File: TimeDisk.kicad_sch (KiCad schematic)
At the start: 72 parts, among them J1 AppleIIBus, J2 microUSB, J3 JTAG, SW1 Mode, U1 EPM7128SL84, U2 DS1315S-5, U3 74LVC04AD, U4 AS6C8008, U5 39F040, U6 XC6206P332MR, U7 CH340G, U8 74LVC1G74DC, U9 74AHCT1G125GW, Y1 32k768, Y2 12M

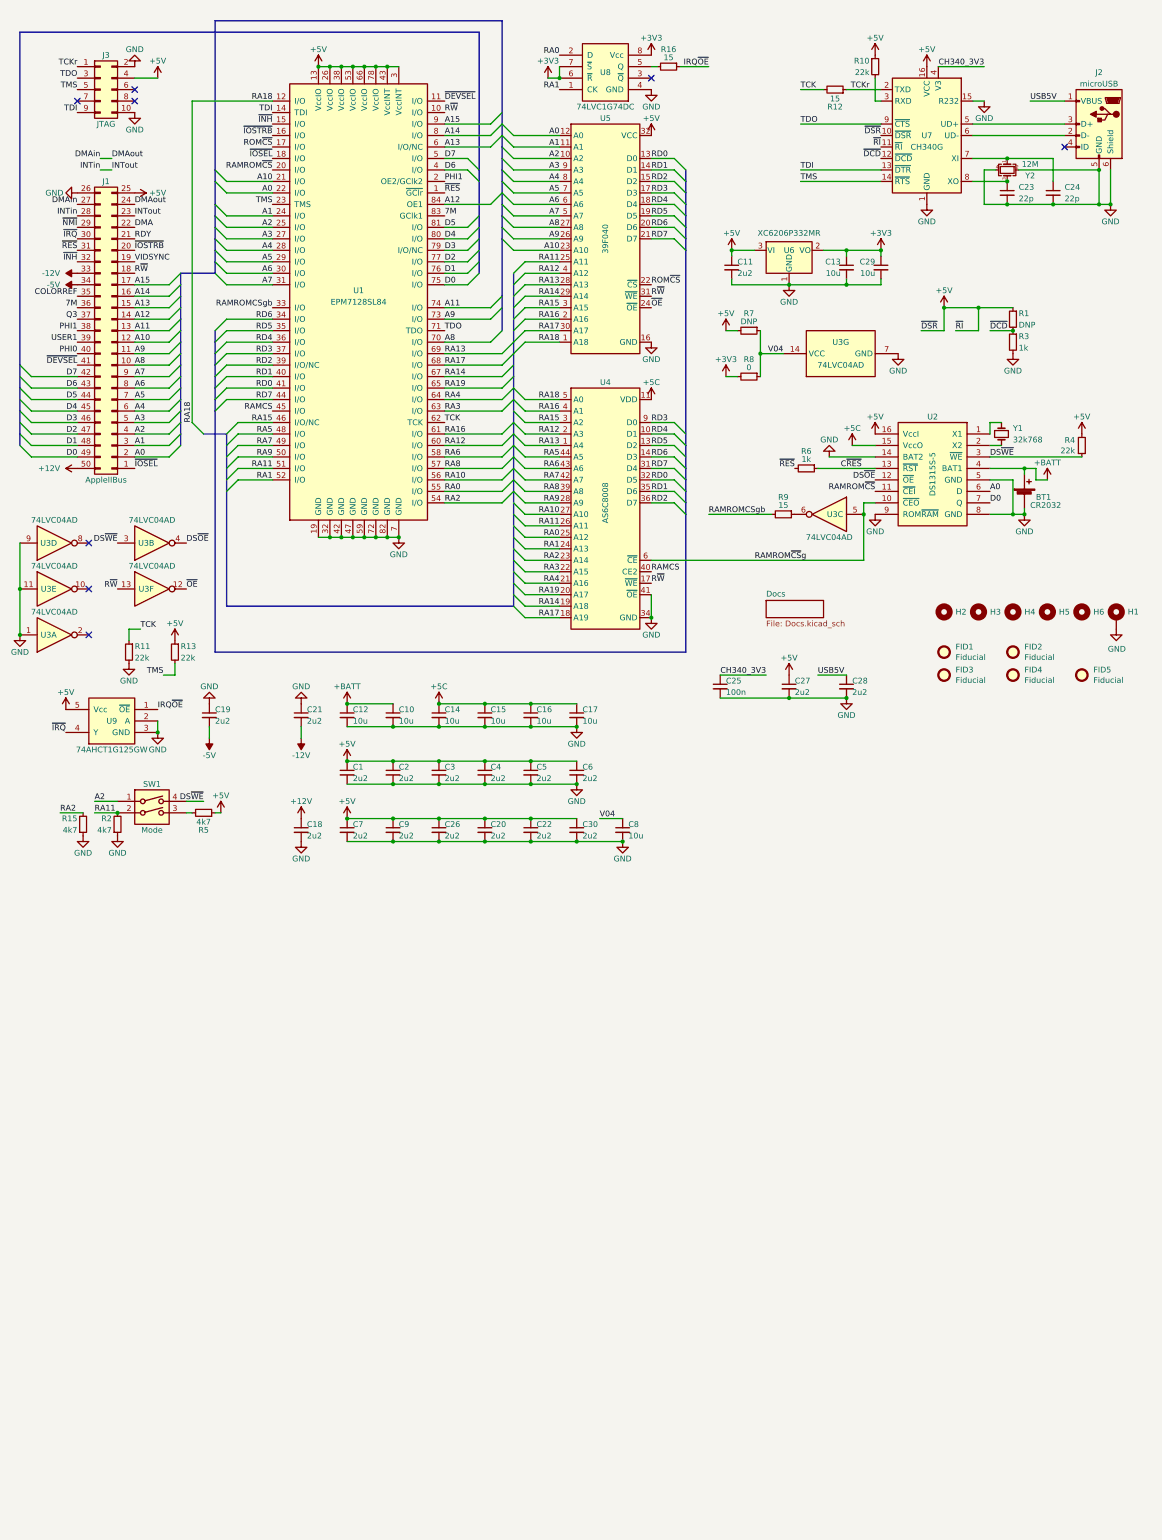
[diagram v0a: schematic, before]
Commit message: Start C revision
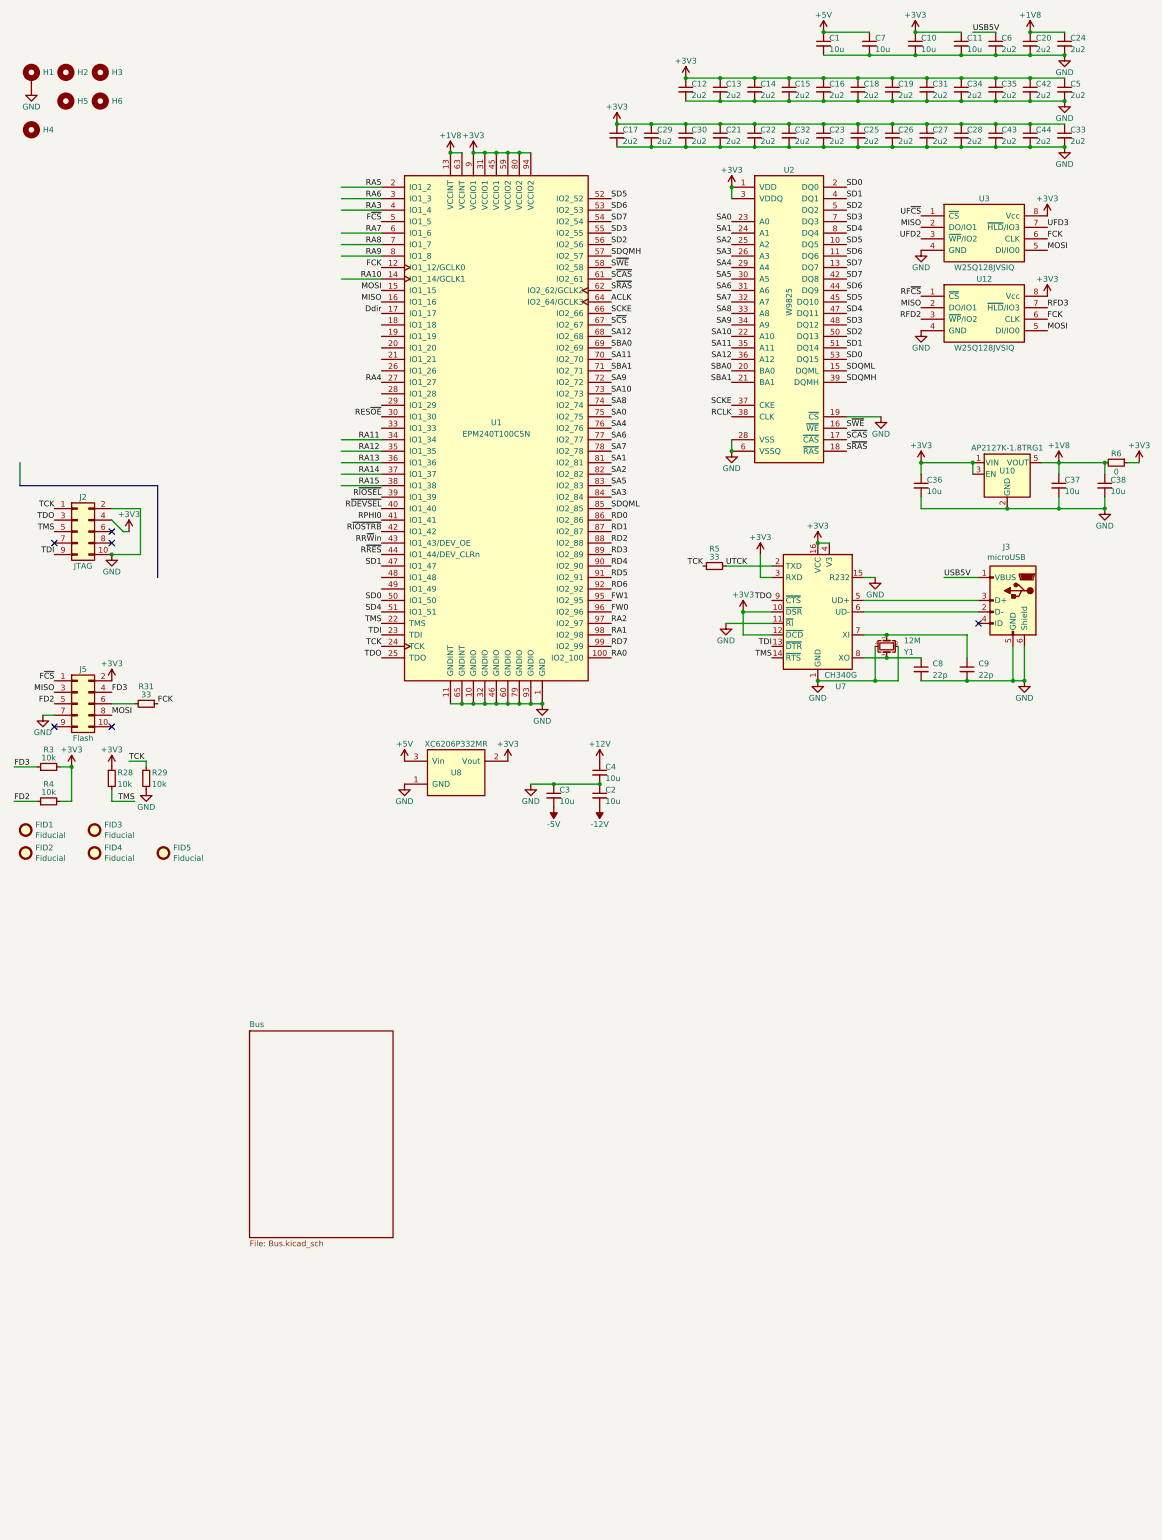
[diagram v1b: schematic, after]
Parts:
- removed BT1: CR2032, stdpads:Keystone_3034_2032, symbol Device:Battery_Cell
- removed C2, C3, C4: 2u2, stdpads:C_0805, symbol Device:C_Small
- removed J1: AppleIIBus, stdpads:AppleIIBus_Edge, symbol Connector_Generic:Conn_02x25_Counter_Clockwise
- removed J2: microUSB, stdpads:USB_Micro-B_Amphenol_10118192-0001, symbol Connector:USB_B_Micro
- removed J3: JTAG, stdpads:Header_2x5_Unshrouded_P1.27mm, symbol Connector_Generic:Conn_02x05_Odd_Even
- removed R1, R7: DNP, stdpads:R_0805, symbol Device:R_Small
- removed R10, R11, R13: 22k, stdpads:R_0805, symbol Device:R_Small
- removed R12, R16, R9: 15, stdpads:R_0805, symbol Device:R_Small
- removed R15, R2: 4k7, stdpads:R_0805, symbol Device:R_Small
- removed R8: 0, stdpads:R_0805, symbol Device:R_Small
- removed SW1: Mode, stdpads:SW_DIP_SPSTx02_Slide_DSHP02TS_P1.27mm, symbol Switch:SW_DIP_x02
- removed U1: EPM7128SL84, stdpads:PLCC-84, symbol GW_PLD:EPM7128SL84
- removed U2: DS1315S-5, stdpads:SOIC-16_7.5mm, symbol GW_Digital:DS1315
- removed U3: 74LVC04AD, stdpads:SOIC-14_3.9mm, symbol 74xx:74HC04
- removed U4: AS6C8008, stdpads:TSOP-II-44_400mil_P0.8mm, symbol GW_RAM:SRAM-1Mx8-TSOP2-44
- removed U5: 39F040, stdpads:PLCC-32_SMDSocket, symbol GW_RAM:Flash-512Kx8-PLCC-32
- removed U6: XC6206P332MR, stdpads:SOT-23, symbol Regulator_Linear:XC6206PxxxMR
- removed U8: 74LVC1G74DC, stdpads:NXP_VSSOP-8_2.3x2mm, symbol GW_Logic:741G74DC
- removed U9: 74AHCT1G125GW, stdpads:SOT-353, symbol GW_Logic:741G125GW
- removed Y1: 32k768, Crystal:Crystal_C26-LF_D2.1mm_L6.5mm_Horizontal, symbol Device:Crystal_Small
- removed Y2: 12M, stdpads:Crystal_SMD_3225-4Pin_3.2x2.5mm, symbol Device:Crystal_GND24_Small
- added C18, C19, C21, C31, C32, C33, C34, C35, C42, C43, C44: 2u2, stdpads:C_0603, symbol Device:C_Small
- added C36, C37, C38: 10u, stdpads:C_0805, symbol Device:C_Small
- added J2: JTAG, Connector:Tag-Connect_TC2050-IDC-FP_2x05_P1.27mm_Vertical, symbol Connector_Generic:Conn_02x05_Odd_Even
- added J3: microUSB, stdpads:USB_Micro-B_Amphenol_10118192-0001, symbol Connector:USB_B_Micro
- added J5: Flash, Connector:Tag-Connect_TC2050-IDC-FP_2x05_P1.27mm_Vertical, symbol Connector_Generic:Conn_02x05_Odd_Even
- added R28, R29: 10k, stdpads:R_0603, symbol Device:R_Small
- added R31: 33, stdpads:R_0603, symbol Device:R_Small
- added U1: EPM240T100C5N, stdpads:TQFP-100_14x14mm_P0.5mm, symbol GW_PLD:5M240ZT100
- added U10: AP2127K-1.8TRG1, stdpads:SOT-23-5, symbol Regulator_Linear:AP2127K-1.8
- added U12, U3: W25Q128JVSIQ, stdpads:SOIC-8_5.3mm, symbol GW_RAM:SPIFlash-SO-8
- added U2: W9825, stdpads:TSOP-II-54_22.2x10.16mm_P0.8mm, symbol GW_RAM:SDRAM-16Mx16-TSOP2-54
- added U8: XC6206P332MR, stdpads:SOT-23, symbol GW_Power:AP2125
- added Y1: 12M, stdpads:Crystal_SMD_3225-4Pin_3.2x2.5mm, symbol Device:Crystal_GND24_Small
- C1, C11, C7: value 2u2 -> 10u; LCSC Part (none) -> C15850
- C10: LCSC Part (none) -> C15850
- C12, C13, C14, C15, C16, C17, C29: value 10u -> 2u2; footprint stdpads:C_0805 -> stdpads:C_0603; LCSC Part (none) -> C23630
- C2: renamed from C21; value 2u2 -> 10u; LCSC Part (none) -> C15850
- C20, C22, C26, C30, C5, C6: footprint stdpads:C_0805 -> stdpads:C_0603; LCSC Part (none) -> C23630
- C23, C24: value 22p -> 2u2; LCSC Part C1653 -> C23630
- C25: value 100n -> 2u2; LCSC Part C28233 -> C23630
- C27, C28: footprint stdpads:C_0805 -> stdpads:C_0603
- C3: renamed from C19; value 2u2 -> 10u; LCSC Part (none) -> C15850
- C4: renamed from C18; value 2u2 -> 10u; LCSC Part (none) -> C15850
- C8: value 10u -> 22p; footprint stdpads:C_0805 -> stdpads:C_0603; LCSC Part (none) -> C1653
- C9: value 2u2 -> 22p; footprint stdpads:C_0805 -> stdpads:C_0603; LCSC Part (none) -> C1653
- R3: value 1k -> 10k; footprint stdpads:R_0805 -> stdpads:R_0603; LCSC Part (none) -> 10k
- R4: value 22k -> 10k; footprint stdpads:R_0805 -> stdpads:R_0603; LCSC Part (none) -> 10k
- R5: value 4k7 -> 33; footprint stdpads:R_0805 -> stdpads:R_0603; LCSC Part (none) -> C23140
- R6: value 1k -> 0; LCSC Part (none) -> C17477; Mfg. Part Numbers (none) -> Uniroyal 0805W8F0000T5E; Notes (none) -> Any manufacturer's part is acceptable.
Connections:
- net +5C is gone; now on net +3V3: C14.1, C15.1, C16.1, C17.1
- net +BATT is gone; now on net +3V3: C10.1, C12.1
- net CH340_3V3 is gone; now on net +3V3: C25.1, U7.4 (V3)
- net C~{RES} is gone; now on net +3V3: R6.1
- net V04 is gone; now on an unnamed net: C8.1
- net +3V3: now also C11.1, C22.1, C23.1, C26.1, C27.1, C28.1, C30.1, C5.1, R3.2, R4.2, U7.10 (~{DSR}), U7.12 (~{DCD}), U7.16 (VCC), U7.3 (RXD), C18.1, C19.1, C21.1, C31.1, C32.1, C33.1, C34.1, C35.1, C36.1, C42.1, C43.1, C44.1, J2.4 (Pin_4), J5.2 (Pin_2), R28.1, U1.31 (VCCIO1), U1.45 (VCCIO1), U1.59 (VCCIO2), U1.80 (VCCIO2), U1.9 (VCCIO1), U1.94 (VCCIO2), U10.1 (VIN), U10.3 (EN), U12.8 (Vcc), U2.1 (VDD), U2.14 (VDD), U2.27 (VDD), U2.3 (VDDQ), U2.43 (VDDQ), U2.49 (VDDQ), U2.9 (VDDQ), U3.8 (Vcc), U8.2 (Vout)
- net +5V: now also U8.3 (Vin); no longer C11.1, C20.1, C22.1, C26.1, C27.1, C30.1, C5.1, C6.1, C9.1, R4.2, R5.1, U7.10 (~{DSR}), U7.11 (~{RI}), U7.16 (VCC)
- net GND: now also U7.11 (~{RI}), C18.2, C19.2, C21.2, C31.2, C32.2, C33.2, C34.2, C35.2, C36.2, C37.2, C38.2, C42.2, C43.2, C44.2, J2.10 (Pin_10), J2.2 (Pin_2), J3.5 (GND), J3.6 (Shield), J5.7 (Pin_7), R29.2, U1.1 (GND), U1.10 (GNDIO), U1.11 (GNDINT), U1.32 (GNDIO), U1.46 (GNDIO), U1.60 (GNDIO), U1.65 (GNDINT), U1.79 (GNDIO), U1.93 (GNDIO), U10.2 (GND), U12.4 (GND), U2.12 (VSSQ), U2.19 (~{CS}), U2.28 (VSS), U2.41 (VSS), U2.46 (VSSQ), U2.52 (VSSQ), U2.54 (VSS), U2.6 (VSSQ), U3.4 (GND), U8.1 (GND), Y1.2, Y1.4; no longer R3.2
- net RA0: now also U1.100 (IO2_100)
- net RA1: now also U1.98 (IO2_98)
- net RA10: now also U1.14 (IO1_14/GCLK1)
- net RA11: now also U1.34 (IO1_34)
- net RA12: now also U1.35 (IO1_35)
- net RA13: now also U1.36 (IO1_36)
- net RA14: now also U1.37 (IO1_37)
- net RA15: now also U1.38 (IO1_38)
- net RA2: now also U1.97 (IO2_97)
- net RA3: now also U1.4 (IO1_4)
- net RA4: now also U1.27 (IO1_27)
- net RA5: now also U1.2 (IO1_2)
- net RA6: now also U1.3 (IO1_3)
- net RA7: now also U1.6 (IO1_6)
- net RA8: now also U1.7 (IO1_7)
- net RA9: now also U1.8 (IO1_8)
- net RD0: now also U1.86 (IO2_86)
- net RD1: now also U1.87 (IO2_87)
- net RD2: now also U1.88 (IO2_88)
- net RD3: now also U1.89 (IO2_89)
- net RD4: now also U1.90 (IO2_90)
- net RD5: now also U1.91 (IO2_91)
- net RD6: now also U1.92 (IO2_92)
- net RD7: now also U1.99 (IO2_99)
- net TCK: now also R5.2, J2.1 (Pin_1), R29.1, U1.24 (TCK)
- net TDI: now also J2.9 (Pin_9), U1.23 (TDI)
- net TDO: now also J2.3 (Pin_3), U1.25 (TDO)
- net TMS: now also J2.5 (Pin_5), R28.2, U1.22 (TMS)
- net USB5V: now also C6.1, J3.1 (VBUS); no longer C28.1
- net at U7.6 (UD-): now also J3.2 (D-)
- net at U7.5 (UD+): now also J3.3 (D+)
- net at U7.7 (XI): now also C9.1, Y1.1; no longer C24.1
- net at U7.8 (XO): now also Y1.3; no longer C23.1
- net DS~{WE} renamed FD2
- net FD2: now also J5.5 (Pin_5)
- net TCKr renamed UTCK
- net UTCK: now also R5.1
- net ~{DCD} renamed FD3
- net FD3: now also J5.4 (Pin_4); no longer U7.12 (~{DCD})
- net ~{RES} renamed +1V8
- net +1V8: now also C20.1, C24.1, C37.1, C38.1, U1.13 (VCCINT), U1.63 (VCCINT), U10.5 (VOUT)
- new net: J5.6 (Pin_6), R31.2
- new net ACLK: U1.64 (IO2_64/GCLK3)
- new net Ddir: U1.17 (IO1_17)
- new net FCK: R31.1, U1.12 (IO1_12/GCLK0), U12.6 (CLK), U3.6 (CLK)
- new net FW0: U1.96 (IO2_96)
- new net FW1: U1.95 (IO2_95)
- new net F~{CS}: J5.1 (Pin_1), U1.5 (IO1_5)
- new net MISO: J5.3 (Pin_3), U1.16 (IO1_16), U12.2 (DO/IO1), U3.2 (DO/IO1)
- new net MOSI: J5.8 (Pin_8), U1.15 (IO1_15), U12.5 (DI/IO0), U3.5 (DI/IO0)
- new net RCLK: U2.38 (CLK)
- new net RES~{OE}: U1.30 (IO1_30)
- new net RFD2: U12.3 (~{WP}/IO2)
- new net RFD3: U12.7 (~{HLD}/IO3)
- new net RF~{CS}: U12.1 (~{CS})
- new net RPHI0: U1.41 (IO1_41)
- new net RR~{W}in: U1.43 (IO1_43/DEV_OE)
- new net R~{DEVSEL}: U1.40 (IO1_40)
- new net R~{IOSEL}: U1.39 (IO1_39)
- new net R~{IOSTRB}: U1.42 (IO1_42)
- new net R~{RES}: U1.44 (IO1_44/DEV_CLRn)
- new net SA0: U1.75 (IO2_75), U2.23 (A0)
- new net SA1: U1.81 (IO2_81), U2.24 (A1)
- new net SA10: U1.73 (IO2_73), U2.22 (A10)
- new net SA11: U1.70 (IO2_70), U2.35 (A11)
- new net SA12: U1.68 (IO2_68), U2.36 (A12)
- new net SA2: U1.82 (IO2_82), U2.25 (A2)
- new net SA3: U1.84 (IO2_84), U2.26 (A3)
- new net SA4: U1.76 (IO2_76), U2.29 (A4)
- new net SA5: U1.83 (IO2_83), U2.30 (A5)
- new net SA6: U1.77 (IO2_77), U2.31 (A6)
- new net SA7: U1.78 (IO2_78), U2.32 (A7)
- new net SA8: U1.74 (IO2_74), U2.33 (A8)
- new net SA9: U1.72 (IO2_72), U2.34 (A9)
- new net SBA0: U1.69 (IO2_69), U2.20 (BA0)
- new net SBA1: U1.71 (IO2_71), U2.21 (BA1)
- new net SCKE: U1.66 (IO2_66), U2.37 (CKE)
- new net SD0: U1.50 (IO1_50), U2.2 (DQ0), U2.53 (DQ15)
- new net SD1: U1.47 (IO1_47), U2.4 (DQ1), U2.51 (DQ14)
- new net SD2: U1.56 (IO2_56), U2.5 (DQ2), U2.50 (DQ13)
- new net SD3: U1.55 (IO2_55), U2.48 (DQ12), U2.7 (DQ3)
- new net SD4: U1.51 (IO1_51), U2.47 (DQ11), U2.8 (DQ4)
- new net SD5: U1.52 (IO2_52), U2.10 (DQ5), U2.45 (DQ10)
- new net SD6: U1.53 (IO2_53), U2.11 (DQ6), U2.44 (DQ9)
- new net SD7: U1.54 (IO2_54), U2.13 (DQ7), U2.42 (DQ8)
- new net SDQMH: U1.57 (IO2_57), U2.39 (DQMH)
- new net SDQML: U1.85 (IO2_85), U2.15 (DQML)
- new net S~{CAS}: U1.61 (IO2_61), U2.17 (~{CAS})
- new net S~{CS}: U1.67 (IO2_67)
- new net S~{RAS}: U1.62 (IO2_62/GCLK2), U2.18 (~{RAS})
- new net S~{WE}: U1.58 (IO2_58), U2.16 (~{WE})
- new net UFD2: U3.3 (~{WP}/IO2)
- new net UFD3: U3.7 (~{HLD}/IO3)
- new net UF~{CS}: U3.1 (~{CS})
- no-connect marks 8 -> 6
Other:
- removed sheet Docs
- added sheet Bus (Bus.kicad_sch)
- title: Time Machine -> GR8RAM
- moved on the sheet: C2, C3, C4

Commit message: Start on hibernate
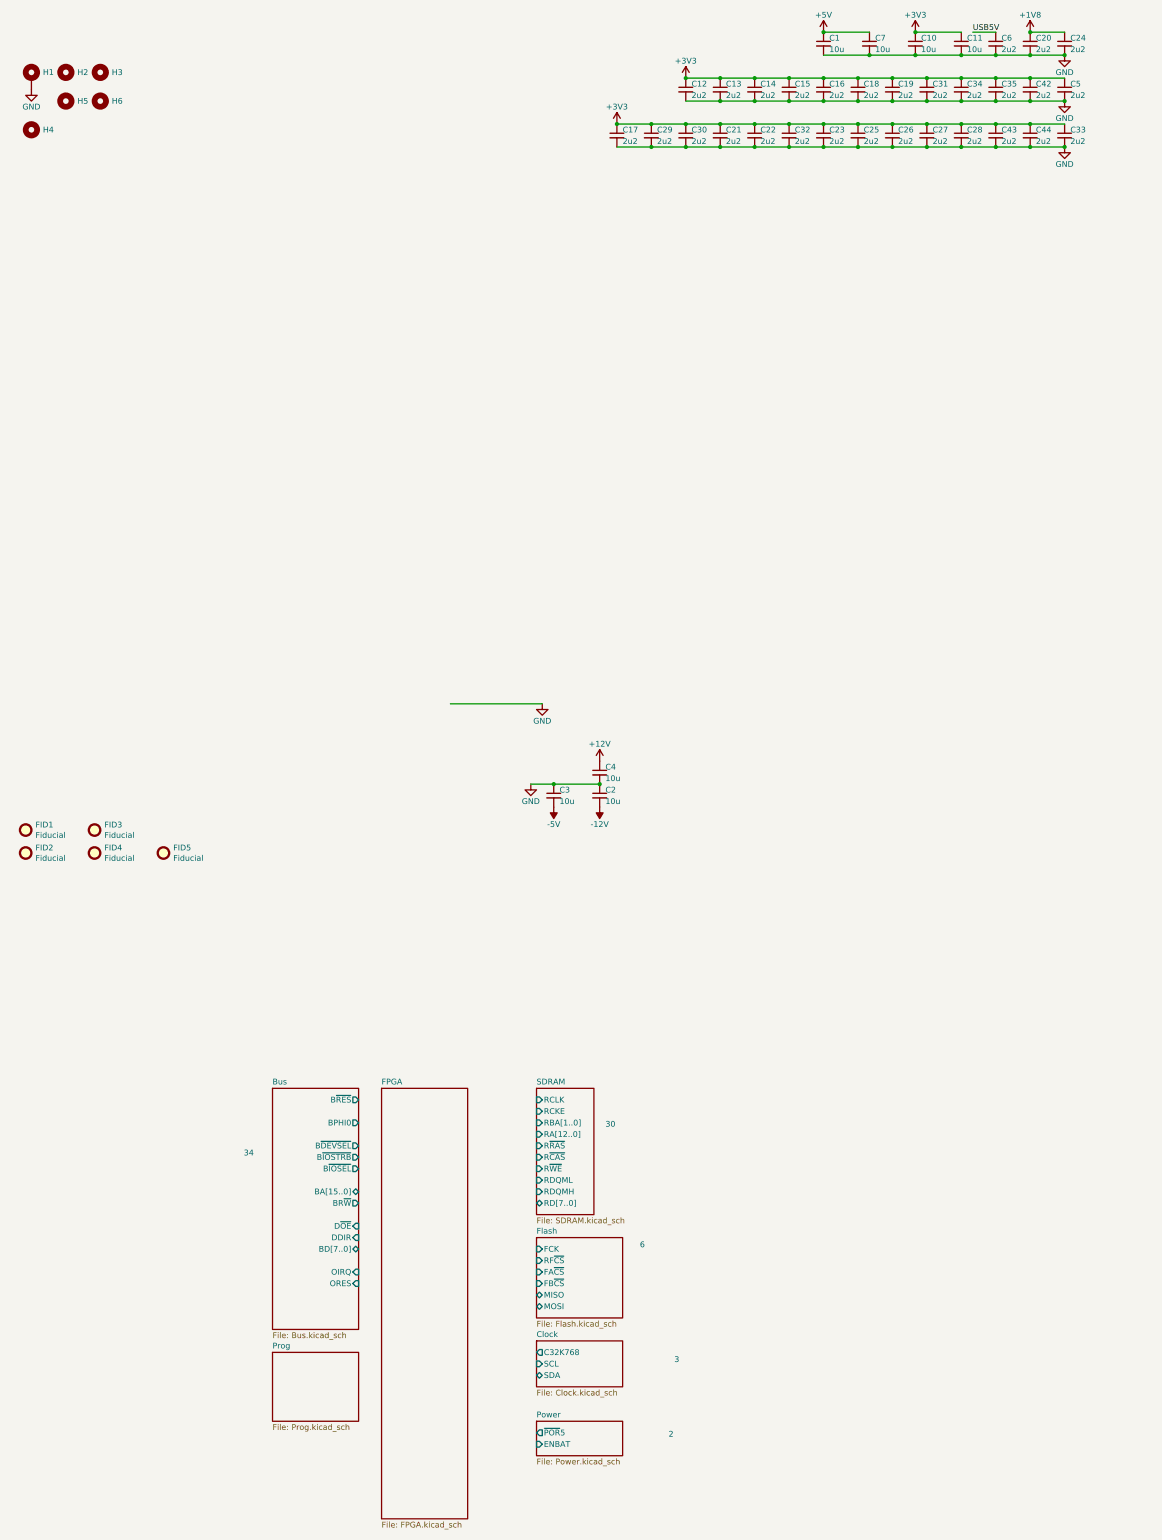
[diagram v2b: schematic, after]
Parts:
- removed C36, C37, C38: 10u, stdpads:C_0805, symbol Device:C_Small
- removed C8, C9: 22p, stdpads:C_0603, symbol Device:C_Small
- removed J2: JTAG, Connector:Tag-Connect_TC2050-IDC-FP_2x05_P1.27mm_Vertical, symbol Connector_Generic:Conn_02x05_Odd_Even
- removed J3: microUSB, stdpads:USB_Micro-B_Amphenol_10118192-0001, symbol Connector:USB_B_Micro
- removed J5: Flash, Connector:Tag-Connect_TC2050-IDC-FP_2x05_P1.27mm_Vertical, symbol Connector_Generic:Conn_02x05_Odd_Even
- removed R28, R29, R3, R4: 10k, stdpads:R_0603, symbol Device:R_Small
- removed R31, R5: 33, stdpads:R_0603, symbol Device:R_Small
- removed R6: 0, stdpads:R_0805, symbol Device:R_Small
- removed U1: EPM240T100C5N, stdpads:TQFP-100_14x14mm_P0.5mm, symbol GW_PLD:5M240ZT100
- removed U10: AP2127K-1.8TRG1, stdpads:SOT-23-5, symbol Regulator_Linear:AP2127K-1.8
- removed U12, U3: W25Q128JVSIQ, stdpads:SOIC-8_5.3mm, symbol GW_RAM:SPIFlash-SO-8
- removed U2: W9825, stdpads:TSOP-II-54_22.2x10.16mm_P0.8mm, symbol GW_RAM:SDRAM-16Mx16-TSOP2-54
- removed U7: CH340G, stdpads:SOIC-16_3.9mm, symbol Interface_USB:CH340G
- removed U8: XC6206P332MR, stdpads:SOT-23, symbol GW_Power:AP2125
- removed Y1: 12M, stdpads:Crystal_SMD_3225-4Pin_3.2x2.5mm, symbol Device:Crystal_GND24_Small
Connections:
- no-connect marks 6 -> 0
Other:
- added sheet Clock (Clock.kicad_sch)
- added sheet FPGA (FPGA.kicad_sch)
- added sheet Flash (Flash.kicad_sch)
- added sheet Power (Power.kicad_sch)
- added sheet Prog (Prog.kicad_sch)
- added sheet SDRAM (SDRAM.kicad_sch)
- sheet Bus ports: added BA[15..0], BD[7..0], BPHI0, BR~{W}, B~{DEVSEL}, B~{IOSEL}, B~{IOSTRB}, B~{RES}, DDIR, D~{OE}, OIRQ, ORES; removed none
- note added: "2"
- note added: "3"
- note added: "30"
- note added: "34"
- note added: "6"

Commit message: idk
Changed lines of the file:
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@@
     )
   )
-  (sheet (at 129.54 325.12) (size 19.05 7.62) (fields_autoplaced)
+  (sheet (at 129.54 322.58) (size 19.05 7.62) (fields_autoplaced)
     (stroke (width 0.1524) (type solid))
     (fill (color 0 0 0 0.0000))
-    (property "Sheetname" "Power" (at 129.54 324.4084 0)
+    (property "Sheetname" "Power" (at 129.54 321.8684 0)
       (effects (font (size 1.27 1.27)) (justify left bottom))
     )
-    (property "Sheetfile" "Power.kicad_sch" (at 129.54 333.3246 0)
+    (property "Sheetfile" "Power.kicad_sch" (at 129.54 330.7846 0)
       (effects (font (size 1.27 1.27)) (justify left top))
     )
-    (pin "~{POR}5" output (at 129.54 327.66 180)
+    (pin "~{POR}5" output (at 129.54 325.12 180)
       (effects (font (size 1.27 1.27)) (justify left))
     )
-    (pin "ENBAT" input (at 129.54 330.2 180)
+    (pin "ENBAT" input (at 129.54 327.66 180)
       (effects (font (size 1.27 1.27)) (justify left))
     )
